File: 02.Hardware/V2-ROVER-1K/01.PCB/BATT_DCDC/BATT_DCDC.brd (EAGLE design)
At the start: 20.4 x 34.4 mm, 60 parts, among them J1 DF40C-20DP-0.4V_51_, K1 FLEX8, Q1 NVTFS9D6P04M8LTAG, Q2 2N7002PW, Q5 2N7002PW, U1 MCP6071T-E/OT, U3 TPS55330RTET, U7 MCP6071T-E/OT

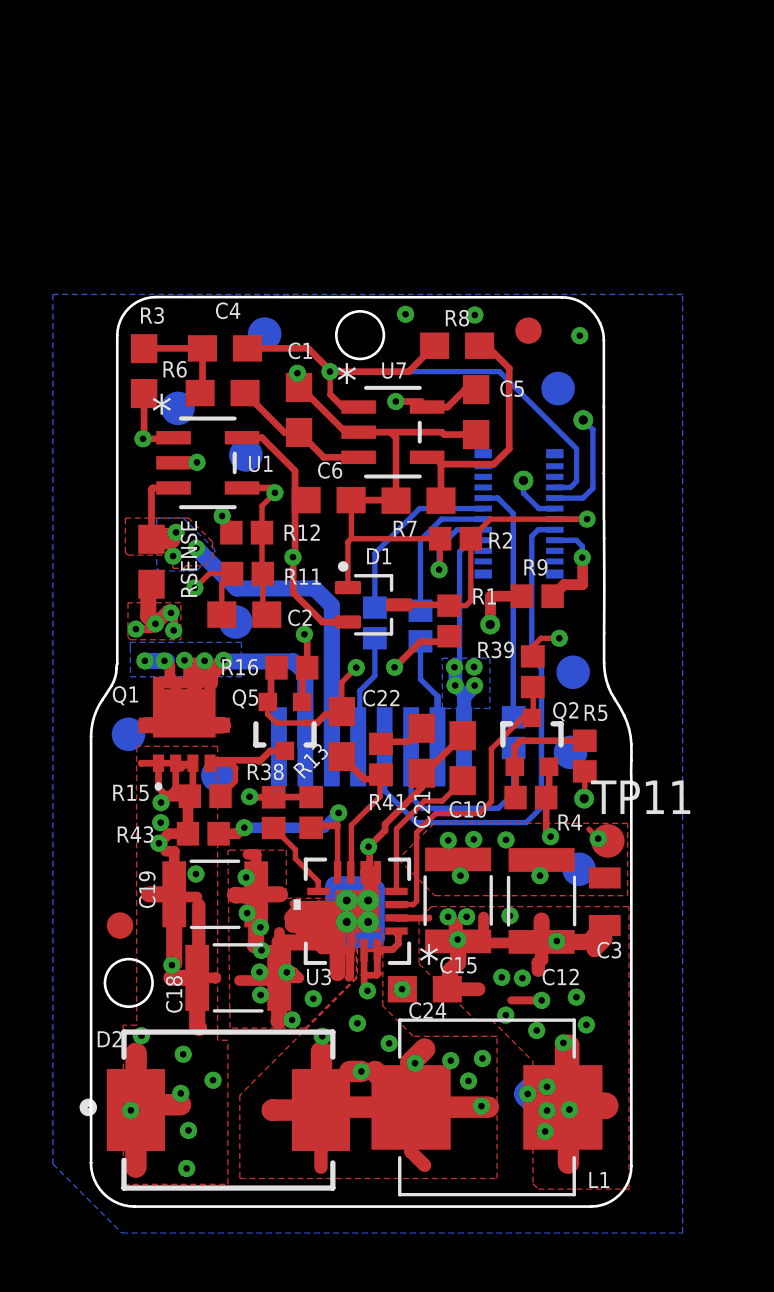
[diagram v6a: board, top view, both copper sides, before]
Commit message: Cambios DCDC Javi Version Final. Pendiente de revision
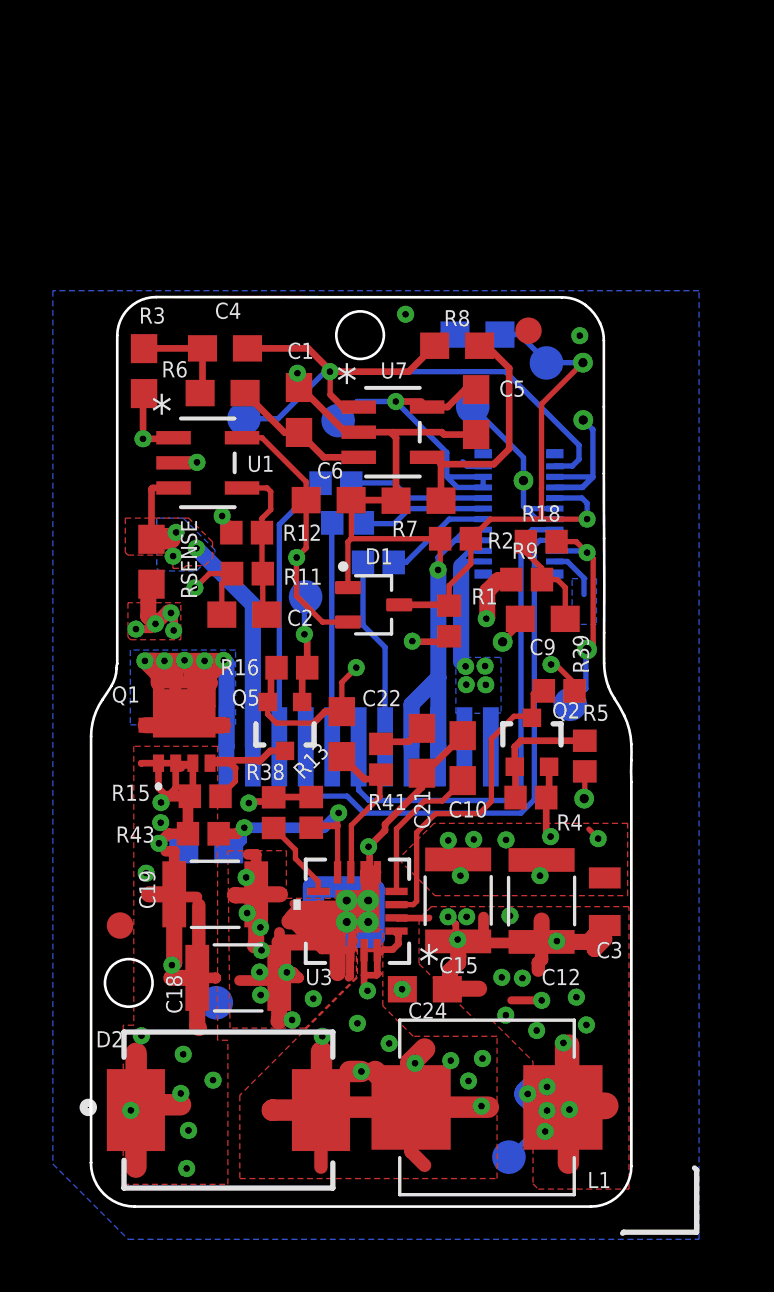
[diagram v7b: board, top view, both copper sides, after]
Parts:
- removed TP1, TP10, TP11, TP2, TP3, TP4, TP5, TP6, TP7, TP8, TP9: TESTPAD_TPSQB1,27, BeagleBone_Blue_R3:TESTPAD_B1,27
- added C7: 220pF, SparkFun-Capacitors:0603
- added C8, C9: 100n, SparkFun-Capacitors:0603
- added EN_DCDC, FB_DAC, GND, IOSENSE, OP_SWITCH, VBUS, VCC, VOUTSENSE: TESTPAD_TPSQB1,27, BeagleBone_Blue_R3:TESTPAD_B1,27
- added R18: 0R, SparkFun-Resistors:0402
- C21: value 2.2nF -> 47nF
- C22: value 270PF -> 100pF
- C24: value 100nF -> 0.1uF
- K1: value FLEX8 -> FLEX11; device Flex_3mm:FLEX8 -> Flex_3mm:FLEX11
- R41: value 56k2 -> 15k
- R7: value 2k4 -> 4k3
- moved R10 10.1 mm to (67.2, 28.0), turned to 0 degrees
- moved R17 5.49 mm to (66.8, 29.5), turned to 0 degrees
- moved R14 2.89 mm to (68.4, 26.5), turned to 0 degrees
- moved R39 1.23 mm to (75.2, 21.7), turned to 180 degrees
- moved K1 1.02 mm to (73.4, 17.5)
- moved R9 0.75 mm to (74.0, 25.9)
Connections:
- removed net VCC_2: J1.6, TP8.TP
- new net N$11: K1.5, R14.2
- new net N$12: C9.1, R18.1, R9.2
- new net RXI: J1.15, K1.9
- net !RESET: now also R17.1; no longer R10.1
- net EN_DCDC: now also EN_DCDC.TP, J1.11; no longer TP6.TP
- net FB: now also C7.1
- net FB_DAC: now also FB_DAC.TP, J1.17, R18.2; no longer J1.15, R9.2, TP2.TP
- net GND: now also C8.2, C9.2, GND.TP, J1.16, J1.2, K1.3, K1.4; no longer K1.9, TP11.TP, TP3.TP
- net IOSENSE: now also IOSENSE.TP, J1.1; no longer J1.5, TP5.TP
- net N$10: now also K1.10; no longer K1.5
- net N$6: now also K1.8; no longer K1.3
- net N$9: now also J1.19; no longer K1.2, R14.2
- net OP_SWITCH: now also J1.3, J1.5, OP_SWITCH.TP; no longer J1.7, TP7.TP
- net SWCLK: now also R10.1; no longer R17.1
- net TXO: now also K1.7; no longer K1.4
- net VBUS: now also J1.18, J1.20, K1.2, VBUS.TP; no longer J1.16, TP1.TP
- net VCC: now also J1.4, J1.6, VCC.TP
- net VOUT+: now also K1.12; no longer K1.8, TP9.TP
- net VOUT-: now also K1.11; no longer K1.7, TP10.TP
- net VOUTSENSE: now also C8.1, J1.7, VOUTSENSE.TP; no longer J1.11, TP4.TP
- net VSOURCE: now also C7.2
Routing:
- net RXI: track 0.00 -> 21.3 mm
- net VOUTSENSE: track 11.1 -> 21.6 mm, vias 1 -> 2
- net VCC: track 39.8 -> 49.4 mm
- net N$11: track 0.00 -> 7.32 mm
- net GND: track 120.0 -> 126.7 mm
- net N$10: track 4.37 -> 10.6 mm
- net EN_DCDC: track 15.9 -> 21.1 mm
- net FB_DAC: track 3.90 -> 8.76 mm, vias 1 -> 2
- net OP_SWITCH: track 24.4 -> 28.4 mm
- net N$12: track 0.00 -> 3.88 mm
- net !RESET: track 9.10 -> 5.23 mm
- net IOSENSE: track 22.8 -> 26.2 mm
- net VBUS: track 55.9 -> 52.5 mm
- net VOUT-: track 15.9 -> 12.9 mm
- net N$9: track 4.26 -> 1.99 mm
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- added copper zone on layer 16, net N$9

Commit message: brd revisado para produccion SETI
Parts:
- C24: value 0.1uF -> 100nF
- C9: value 100n -> N.A.
- moved GND 14.4 mm to (75.8, 14.7)
- moved VBUS 2.77 mm to (76.1, 4.36)
- moved C7 1.23 mm to (61.0, 14.7), turned to 90 degrees
- moved R18 0.49 mm to (74.0, 27.3)
- moved C2 0.34 mm to (63.0, 24.4)
- moved C8 0.30 mm to (72.1, 34.8)
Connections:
- net N$9 renamed SPARE1
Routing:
- net GND: track 126.7 -> 144.0 mm, vias 31 -> 44
- net VBUS: track 52.5 -> 56.4 mm, vias 22 -> 21
- net TXO: track 19.0 -> 16.5 mm, vias 0 -> 2
- net RXI: track 21.3 -> 18.9 mm, vias 0 -> 2
- net FB: track 21.7 -> 24.0 mm
- net VSOURCE: track 32.5 -> 34.7 mm
- net SW2_TPS: track 28.3 -> 29.6 mm
- net VOUTSENSE: track 21.6 -> 20.7 mm
- net VOUT+: track 33.2 -> 32.5 mm, vias 6 -> 5
- net FB_DAC: track 8.76 -> 9.33 mm
